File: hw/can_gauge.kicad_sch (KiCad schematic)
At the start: 13 parts, among them U1 MCP2515-xSO

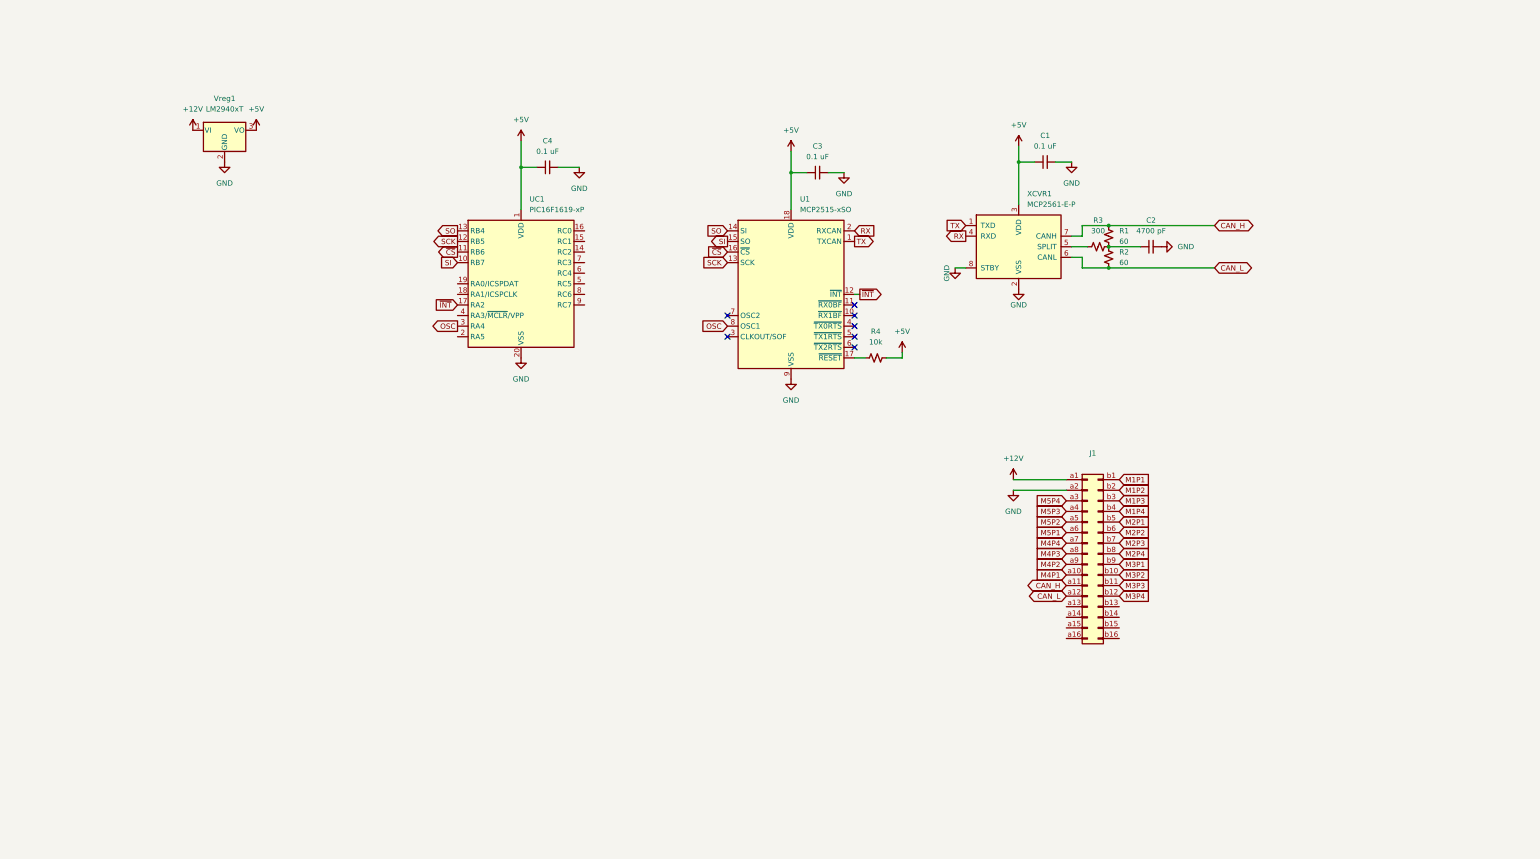
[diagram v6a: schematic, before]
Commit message: hw: motor drivers
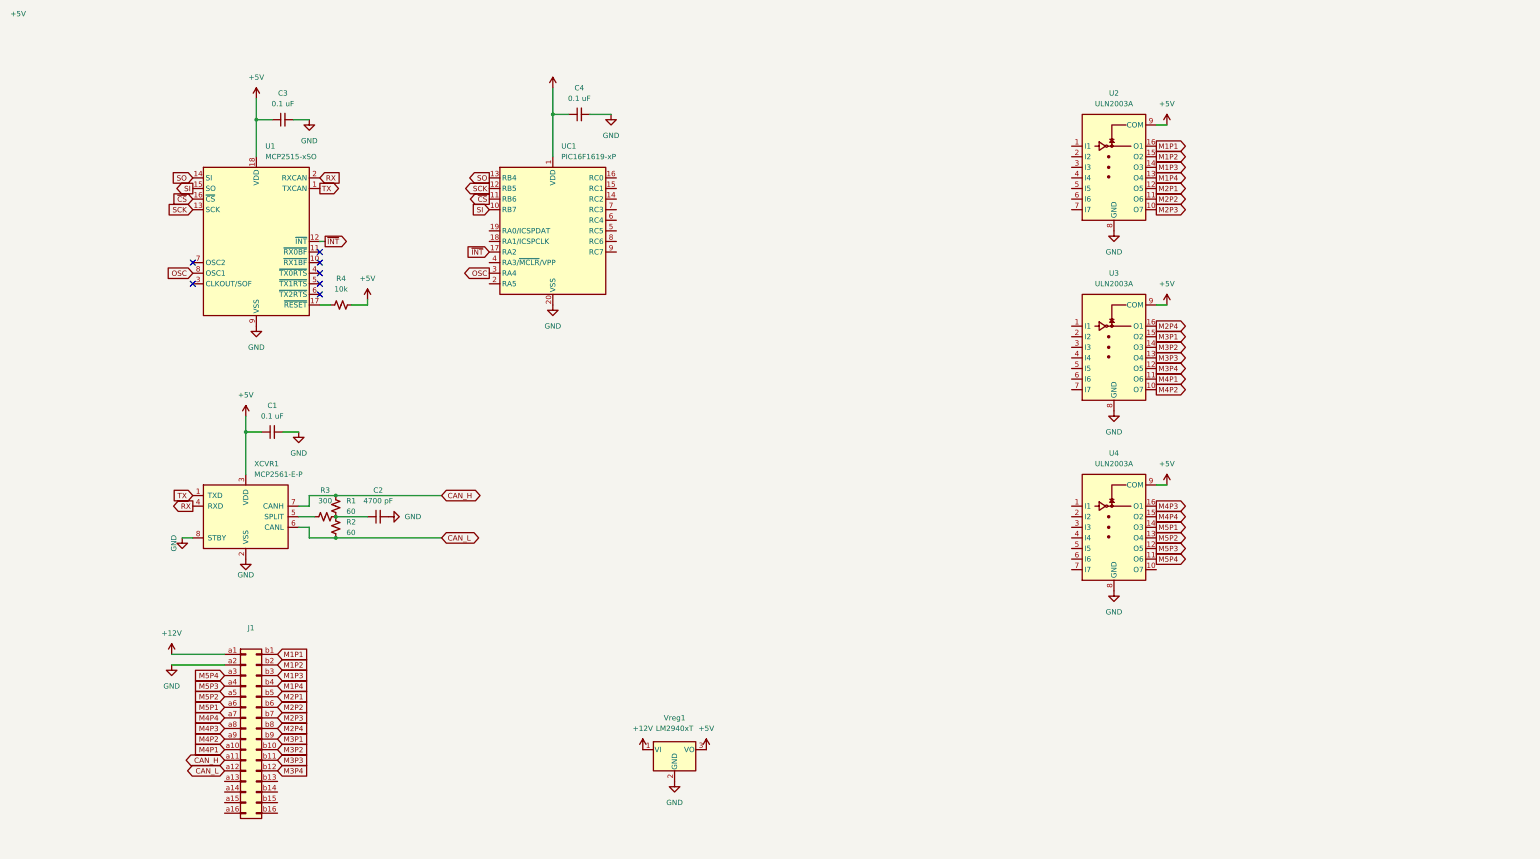
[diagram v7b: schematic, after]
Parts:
- added U2, U3, U4: ULN2003A, symbol Transistor_Array:ULN2003A
- J1: value (none) -> ~
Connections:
- net +5V: now also U2.9 (COM), U3.9 (COM), U4.9 (COM)
- net GND: now also U2.8 (GND), U3.8 (GND), U4.8 (GND)
- net M1P1: now also U2.16 (O1)
- net M1P2: now also U2.15 (O2)
- net M1P3: now also U2.14 (O3)
- net M1P4: now also U2.13 (O4)
- net M2P1: now also U2.12 (O5)
- net M2P2: now also U2.11 (O6)
- net M2P3: now also U2.10 (O7)
- net M2P4: now also U3.16 (O1)
- net M3P1: now also U3.15 (O2)
- net M3P2: now also U3.14 (O3)
- net M3P3: now also U3.13 (O4)
- net M3P4: now also U3.12 (O5)
- net M4P1: now also U3.11 (O6)
- net M4P2: now also U3.10 (O7)
- net M4P3: now also U4.16 (O1)
- net M4P4: now also U4.15 (O2)
- net M5P1: now also U4.14 (O3)
- net M5P2: now also U4.13 (O4)
- net M5P3: now also U4.12 (O5)
- net M5P4: now also U4.11 (O6)
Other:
- moved on the sheet: C1, C2, C3, C4, J1, R1, R2, R3, R4, U1, UC1, Vreg1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

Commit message: hw: shift registers
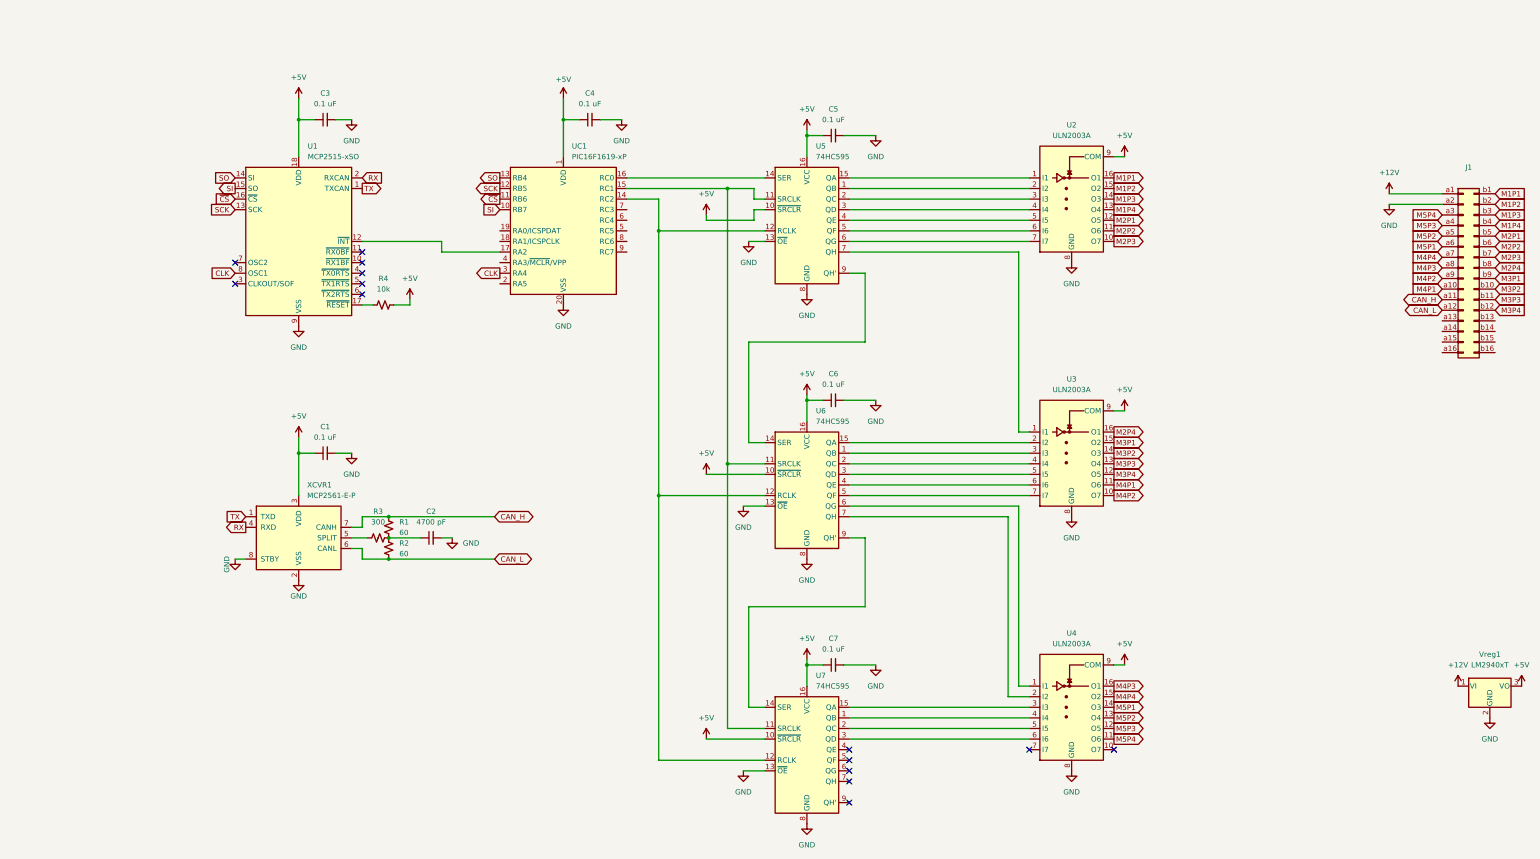
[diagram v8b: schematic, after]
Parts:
- added C5, C6, C7: 0.1 uF, symbol Device:C_Small
- added U5, U6, U7: 74HC595, symbol 74xx:74HC595
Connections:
- net +5V: now also C5.1, C6.1, C7.1, U5.10 (~{SRCLR}), U5.16 (VCC), U6.10 (~{SRCLR}), U6.16 (VCC), U7.10 (~{SRCLR}), U7.16 (VCC)
- net GND: now also C5.2, C6.2, C7.2, U5.13 (~{OE}), U5.8 (GND), U6.13 (~{OE}), U6.8 (GND), U7.13 (~{OE}), U7.8 (GND)
- net at UC1.14 (RC2): now also U5.12 (RCLK), U6.12 (RCLK), U7.12 (RCLK)
- net at UC1.15 (RC1): now also U5.11 (SRCLK), U6.11 (SRCLK), U7.11 (SRCLK)
- net at UC1.16 (RC0): now also U5.14 (SER)
- net at U3.1 (I1): now also U5.7 (QH)
- net at U3.2 (I2): now also U6.15 (QA)
- net at U3.3 (I3): now also U6.1 (QB)
- net at U3.4 (I4): now also U6.2 (QC)
- net at U3.5 (I5): now also U6.3 (QD)
- net at U3.6 (I6): now also U6.4 (QE)
- net at U3.7 (I7): now also U6.5 (QF)
- net at U2.1 (I1): now also U5.15 (QA)
- net at U2.2 (I2): now also U5.1 (QB)
- net at U2.3 (I3): now also U5.2 (QC)
- net at U2.4 (I4): now also U5.3 (QD)
- net at U2.5 (I5): now also U5.4 (QE)
- net at U2.6 (I6): now also U5.5 (QF)
- net at U2.7 (I7): now also U5.6 (QG)
- net at U4.1 (I1): now also U6.6 (QG)
- net at U4.2 (I2): now also U6.7 (QH)
- net at U4.3 (I3): now also U7.15 (QA)
- net at U4.4 (I4): now also U7.1 (QB)
- net at U4.5 (I5): now also U7.2 (QC)
- net at U4.6 (I6): now also U7.3 (QD)
- net OSC renamed CLK
- net ~{INT}: no longer names the net of U1.12 (~{INT}), UC1.17 (RA2)
- new net: U5.9 (QH'), U6.14 (SER)
- new net: U6.9 (QH'), U7.14 (SER)
- no-connect marks 7 -> 14
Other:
- moved on the sheet: C1, C2, C3, C4, J1, R1, R2, R3, R4, U1, U2, U3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
